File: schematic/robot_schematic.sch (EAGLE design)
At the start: 4 parts

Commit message: finished schematic
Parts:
- added M1, M2: MOTOR10MM, SparkFun-Electromechanical:MOTOR10MM
- added U$4: BLUETOOTH, schematic_sym:BLUETOOTH
- added U$5: COLOR_SENSOR, schematic_sym:COLOR_SENSOR
- added U$6: LCD, schematic_sym:LCD
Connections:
- new net BLUE_RX: A1.P13, U$4.RXI
- new net BLUE_TX: A1.P14, U$4.TXO
- new net COLOR_SCL: A1.P10, U$5.SCL
- new net COLOR_SDA: A1.P9, U$5.SDA
- new net I1_ML: A1.P7, U$3.BI1
- new net I1_MR: A1.P5, U$3.AI1
- new net I2_ML: A1.P8, U$3.BI2
- new net I2_MR: A1.P6, U$3.AI2
- new net LCD_RESET: A1.P29, U$6.RES
- new net LCD_RX: A1.P28, U$6.RX
- new net LCD_TX: A1.P27, U$6.TX
- new net N$2: M1.+, U$3.A01
- new net N$3: M1.-, U$3.A02
- new net N$4: M2.+, U$3.B02
- new net N$5: M2.-, U$3.B01
- new net PWM_ML: A1.P22, U$3.PWMB
- new net PWM_MR: A1.P21, U$3.PWMA
- net +3V3: now also U$3.STBY, U$3.VCC, U$5.3V3
- net +5V: now also U$6.+5V
- net GND: now also U$3.GND, U$4.CTS, U$4.GND, U$5.GND, U$6.GND
- net VBATT: now also U$3.VM, U$4.VIN
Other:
- note added: "Bluetooth"
- note added: "Color Sensor"
- note added: "H-Bridge"
- note added: "LCD Screen"
- note added: "Mbed"
- note added: "Power Input"
- moved on the sheet: A1, U$3

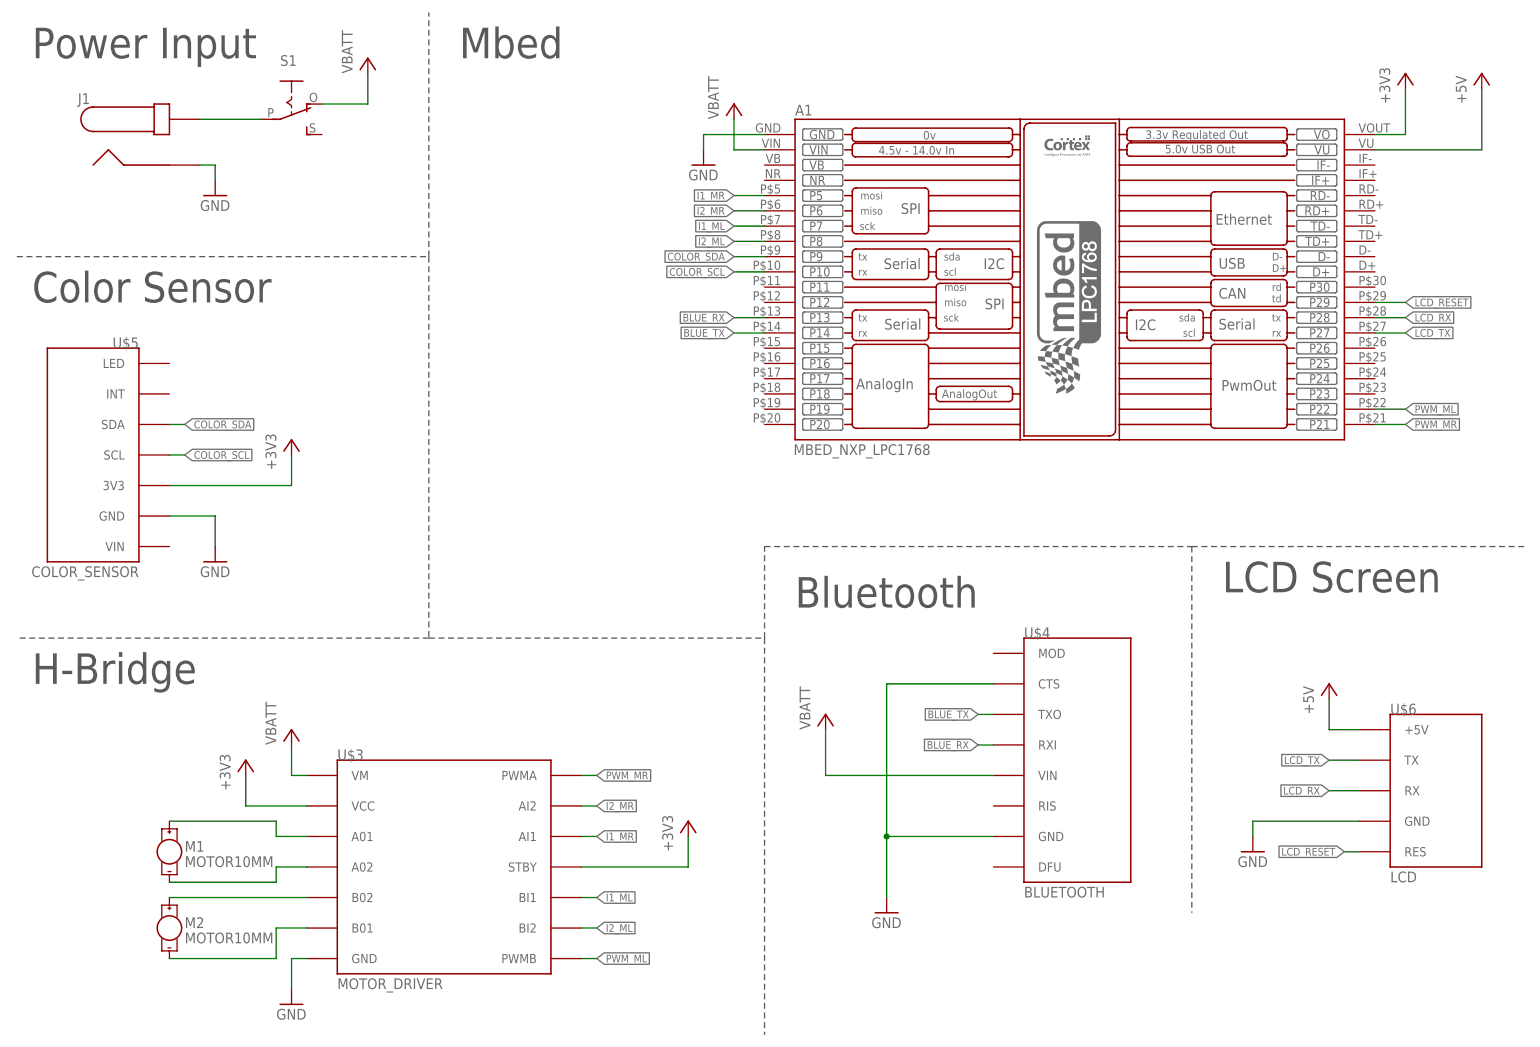
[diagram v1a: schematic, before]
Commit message: added distance sensor to schematic, changed file structure
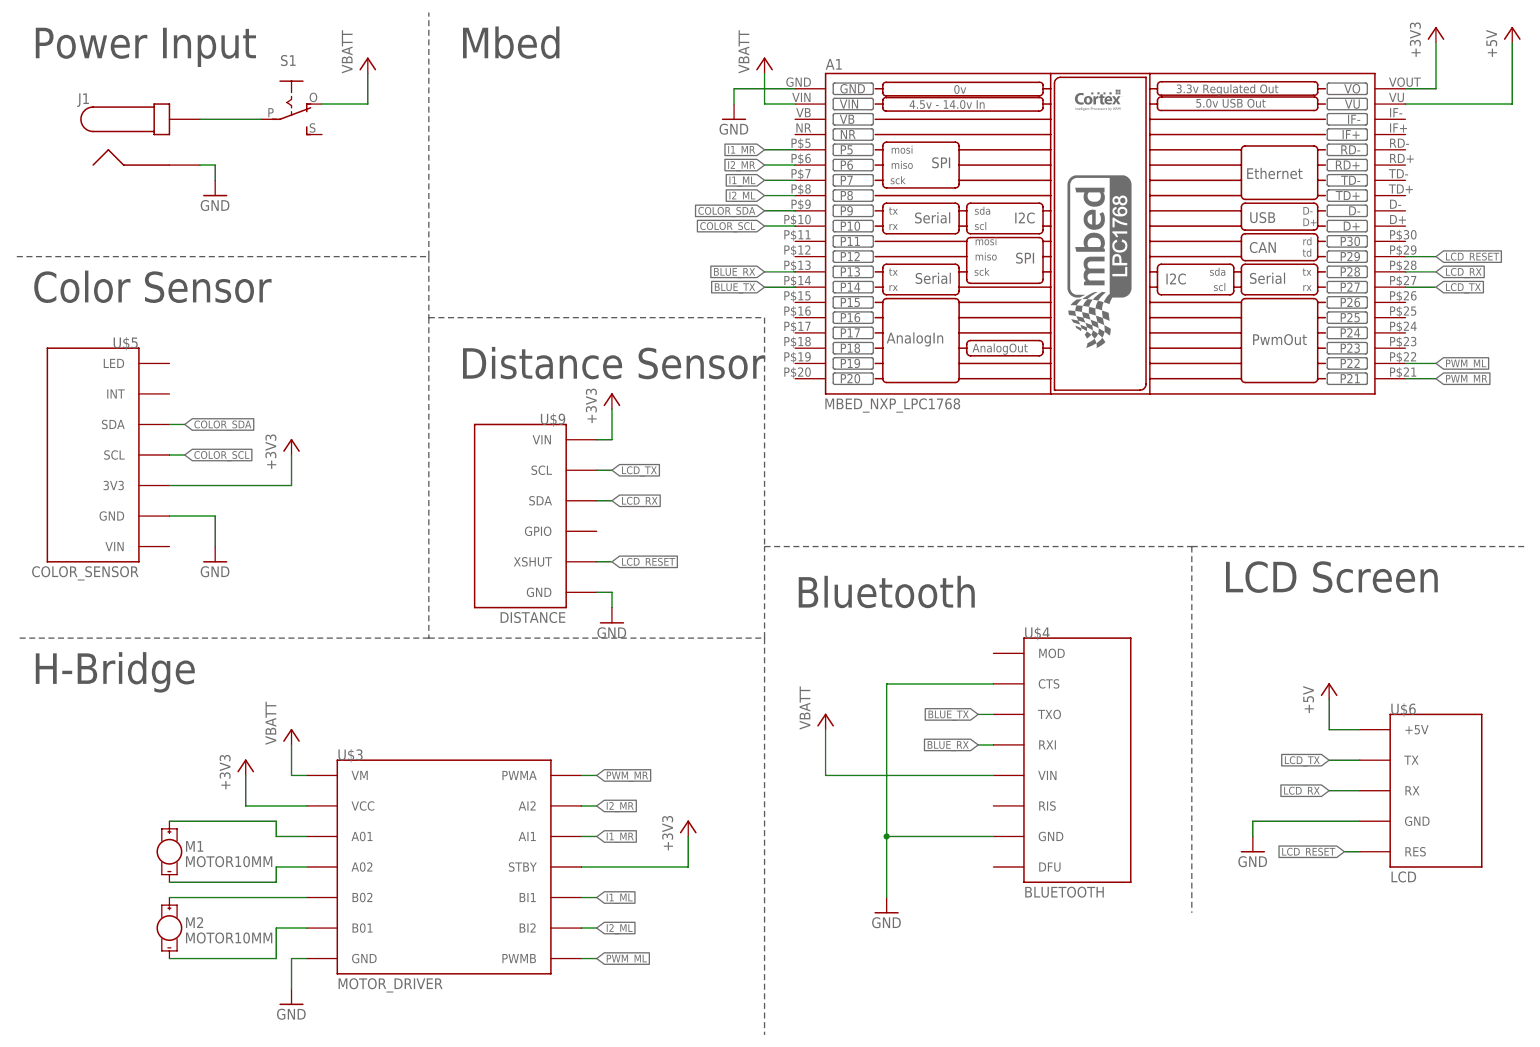
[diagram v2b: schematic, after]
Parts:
- added U$9: DISTANCE, schematic_sym:DISTANCE
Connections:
- net +3V3: now also U$9.VIN
- net GND: now also U$9.GND
- net LCD_RESET: now also U$9.XSHUT
- net LCD_RX: now also U$9.SDA
- net LCD_TX: now also U$9.SCL
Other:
- note added: "Distance Sensor"
- moved on the sheet: A1
